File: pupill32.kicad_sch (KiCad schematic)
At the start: 49 parts, among them J1 HeaderR, J2 HeaderL, J3 USB_PINS, J4 SWD_HEADER, SW1 RST_BTN, SW2 BOOT_BTN, U1 SRV05-4, U2 PY32F030F18P6, U3 CH340N, U4 AMS1117-3.3, Y1 32.768 kHz, Y2 12M

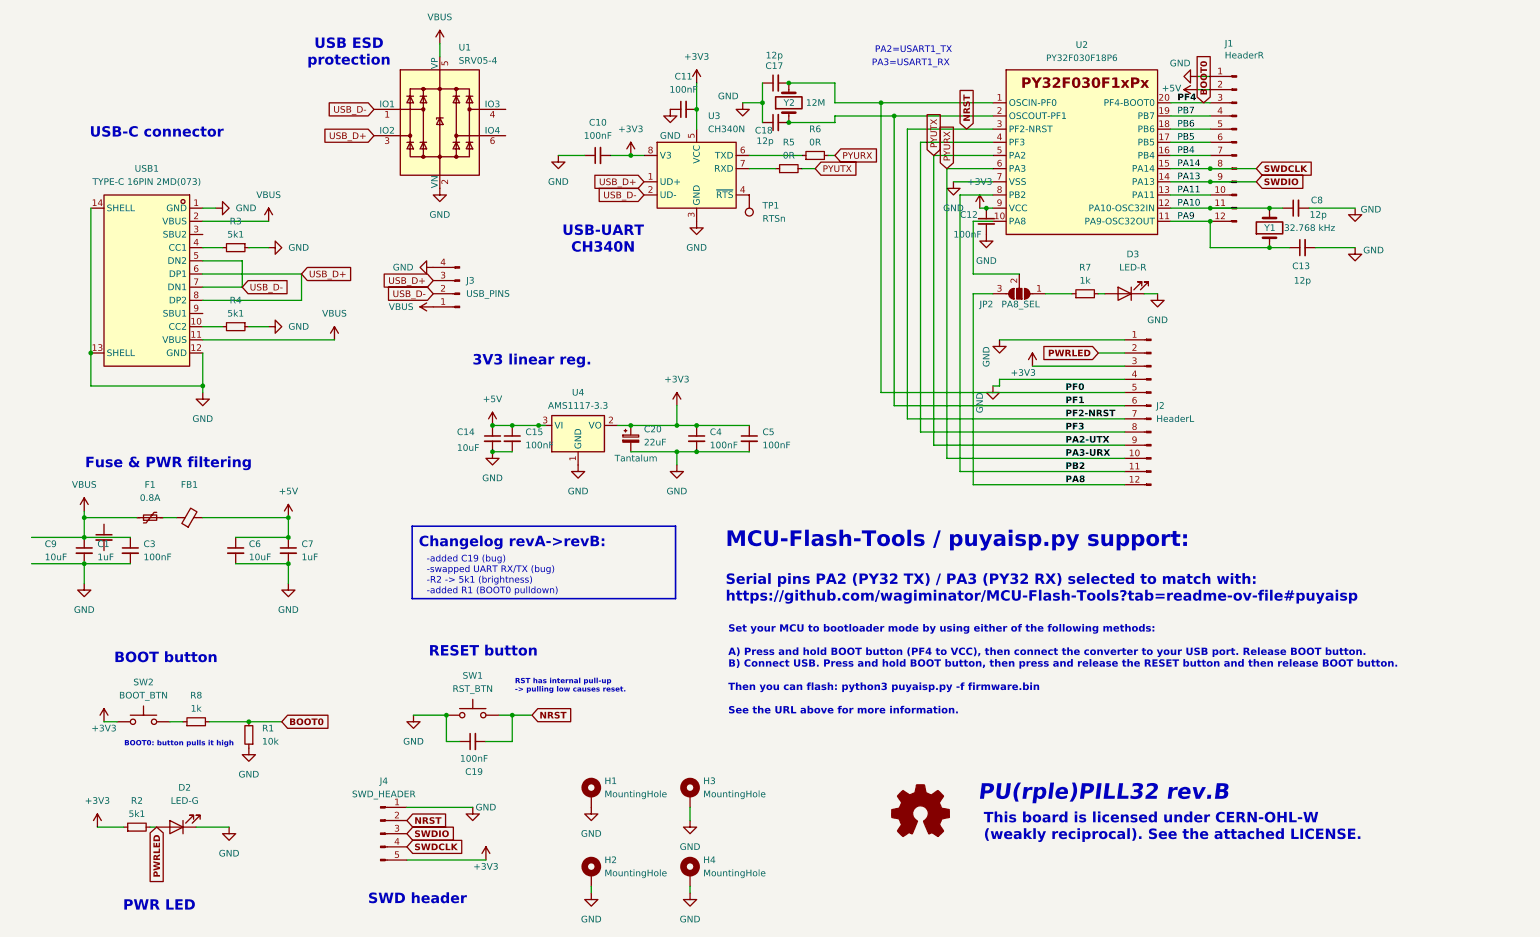
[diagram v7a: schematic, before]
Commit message: SWD resistors, changelog update
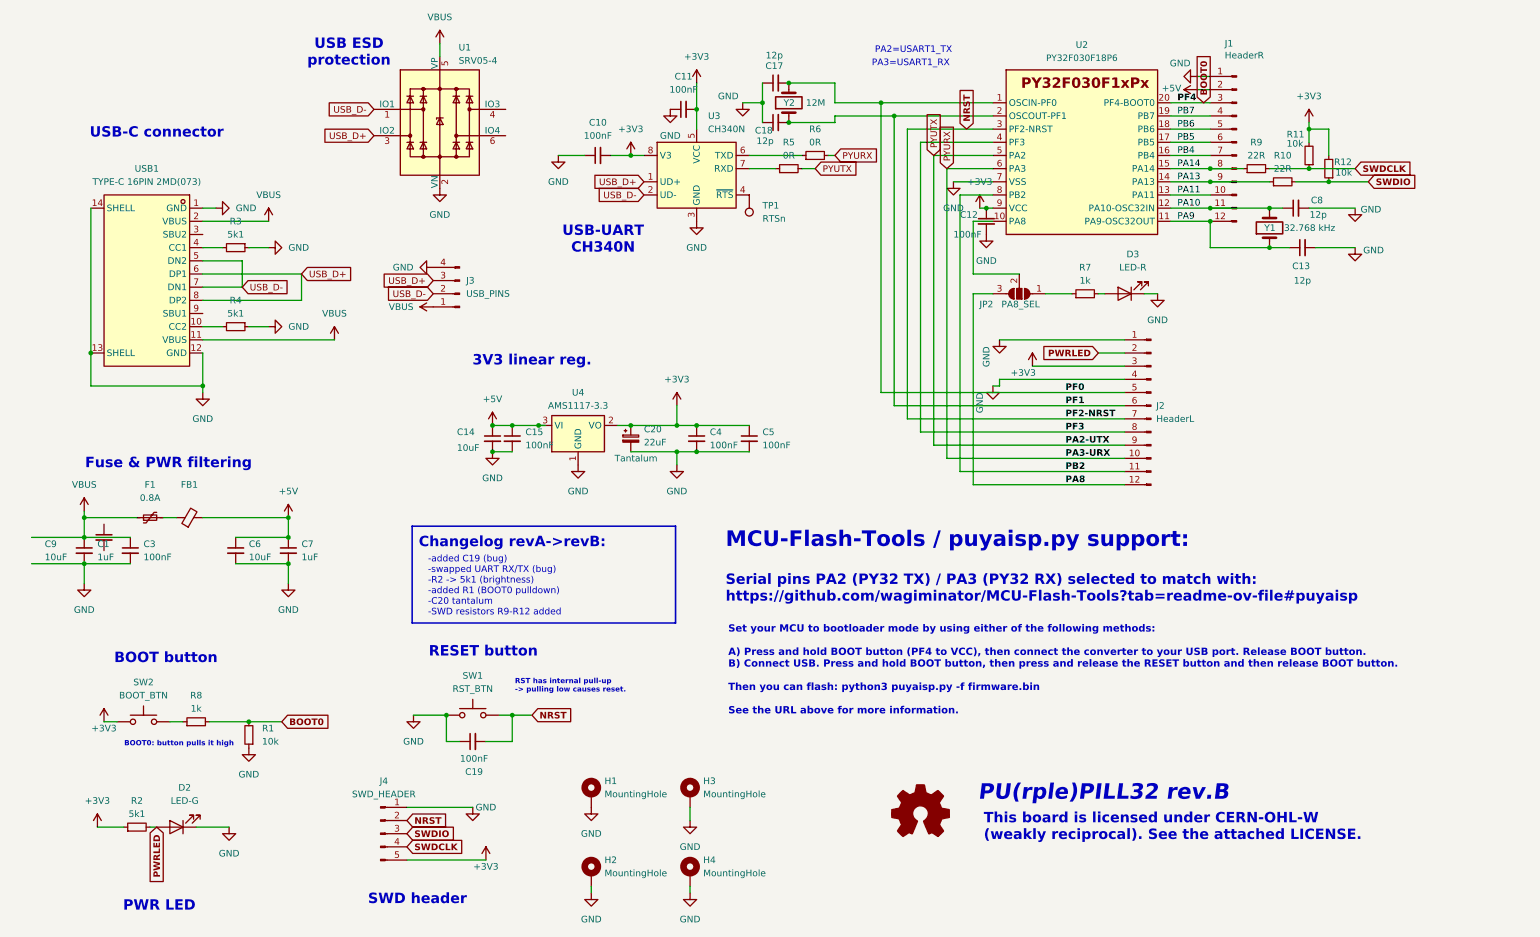
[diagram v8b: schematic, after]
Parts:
- added R10, R9: 22R, Resistor_SMD:R_0805_2012Metric_Pad1.20x1.40mm_HandSolder, symbol Device:R_Small
- added R11, R12: 10k, Resistor_SMD:R_0805_2012Metric_Pad1.20x1.40mm_HandSolder, symbol Device:R_Small
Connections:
- net +3V3: now also R11.2, R12.2
- net SWDCLK: now also R11.1, R9.2; no longer J1.8 (Pin_8), U2.15 (PA14)
- net SWDIO: now also R10.2, R12.1; no longer J1.9 (Pin_9), U2.14 (PA13)
- new net PA13: J1.9 (Pin_9), R10.1, U2.14 (PA13)
- new net PA14: J1.8 (Pin_8), R9.1, U2.15 (PA14)
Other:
- note added: "-added C19 (bug) -swapped UART RX/TX (bug) -R2 -> 5k1 (brightness) -added R1 (BOOT0 pulldown) -C20 tantalum -SWD resistors R9-R12 added"
- note removed: "-added C19 (bug) -swapped UART RX/TX (bug) -R2 -> 5k1 (brightness) -added R1 (BOOT0 pulldown)"
